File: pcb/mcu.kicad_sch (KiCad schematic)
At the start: 31 parts, among them SW1 SKRKAEE020, U10 W25Q128JVS, U8 RP2040, Y3 ABMM2-12.000MHZ-E2-T

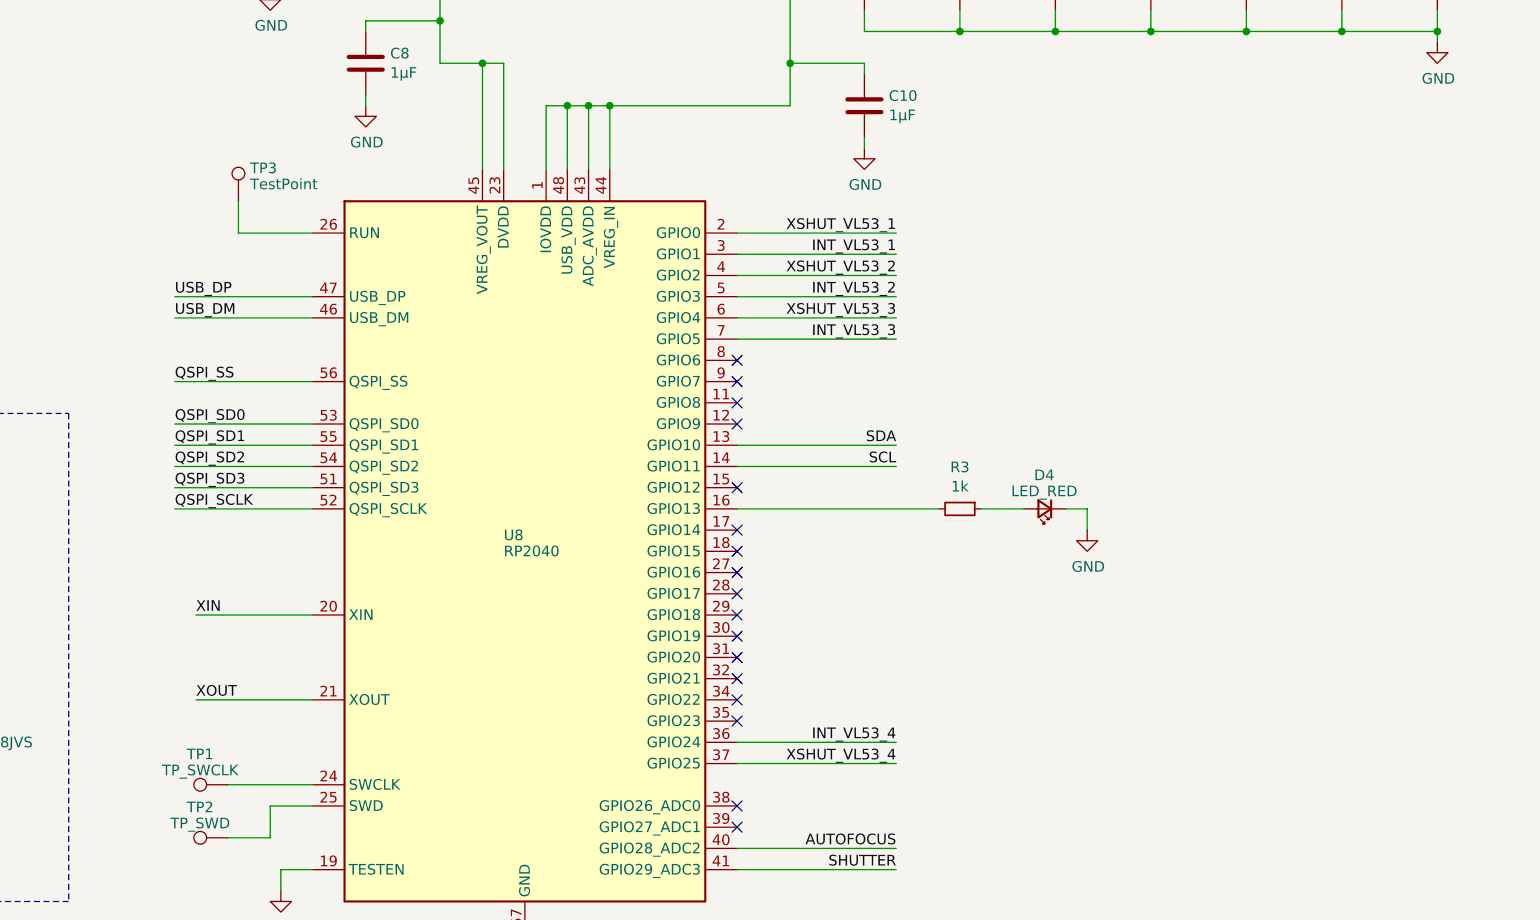
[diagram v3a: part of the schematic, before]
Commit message: refactored components and layout
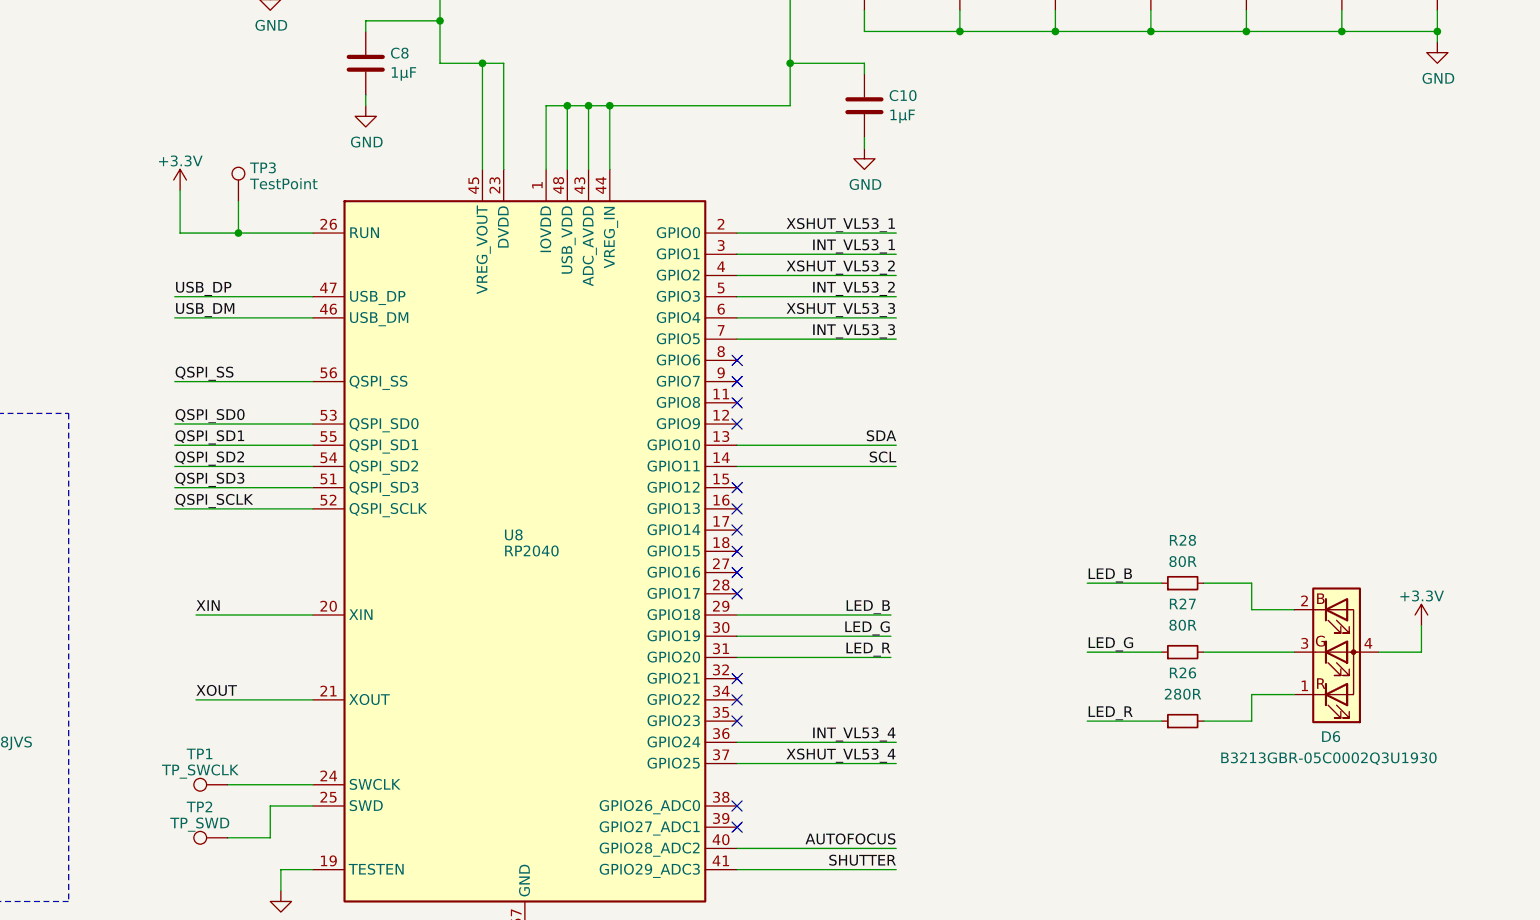
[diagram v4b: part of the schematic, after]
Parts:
- removed D4: LED_RED, LED_SMD:LED_0603_1608Metric, symbol Device:LED_Small
- removed R3: 1k, Resistor_SMD:R_0603_1608Metric, symbol Device:R_Small
- added D6: B3213GBR-05C0002Q3U1930, B3213GBR-05C0002Q3U1930:B3213GBR-05C0002Q3U1930, symbol Device:LED_RBGA
- added R26: 280R, Resistor_SMD:R_0603_1608Metric, symbol Device:R_Small
- added R27, R28: 80R, Resistor_SMD:R_0603_1608Metric, symbol Device:R_Small
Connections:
- net +3.3V: now also TP3.1, U8.26 (RUN), D6.4 (A)
- net LED_B: now reaches U8.29 (GPIO18)
- net LED_B: now also R28.1
- net LED_G: now reaches U8.30 (GPIO19)
- net LED_G: now also R27.1
- net LED_R: now reaches U8.31 (GPIO20)
- net LED_R: now also R26.1
- new net: D6.3 (GK), R27.2
- new net: D6.1 (RK), R26.2
- new net: D6.2 (BK), R28.2
- no-connect marks 17 -> 15

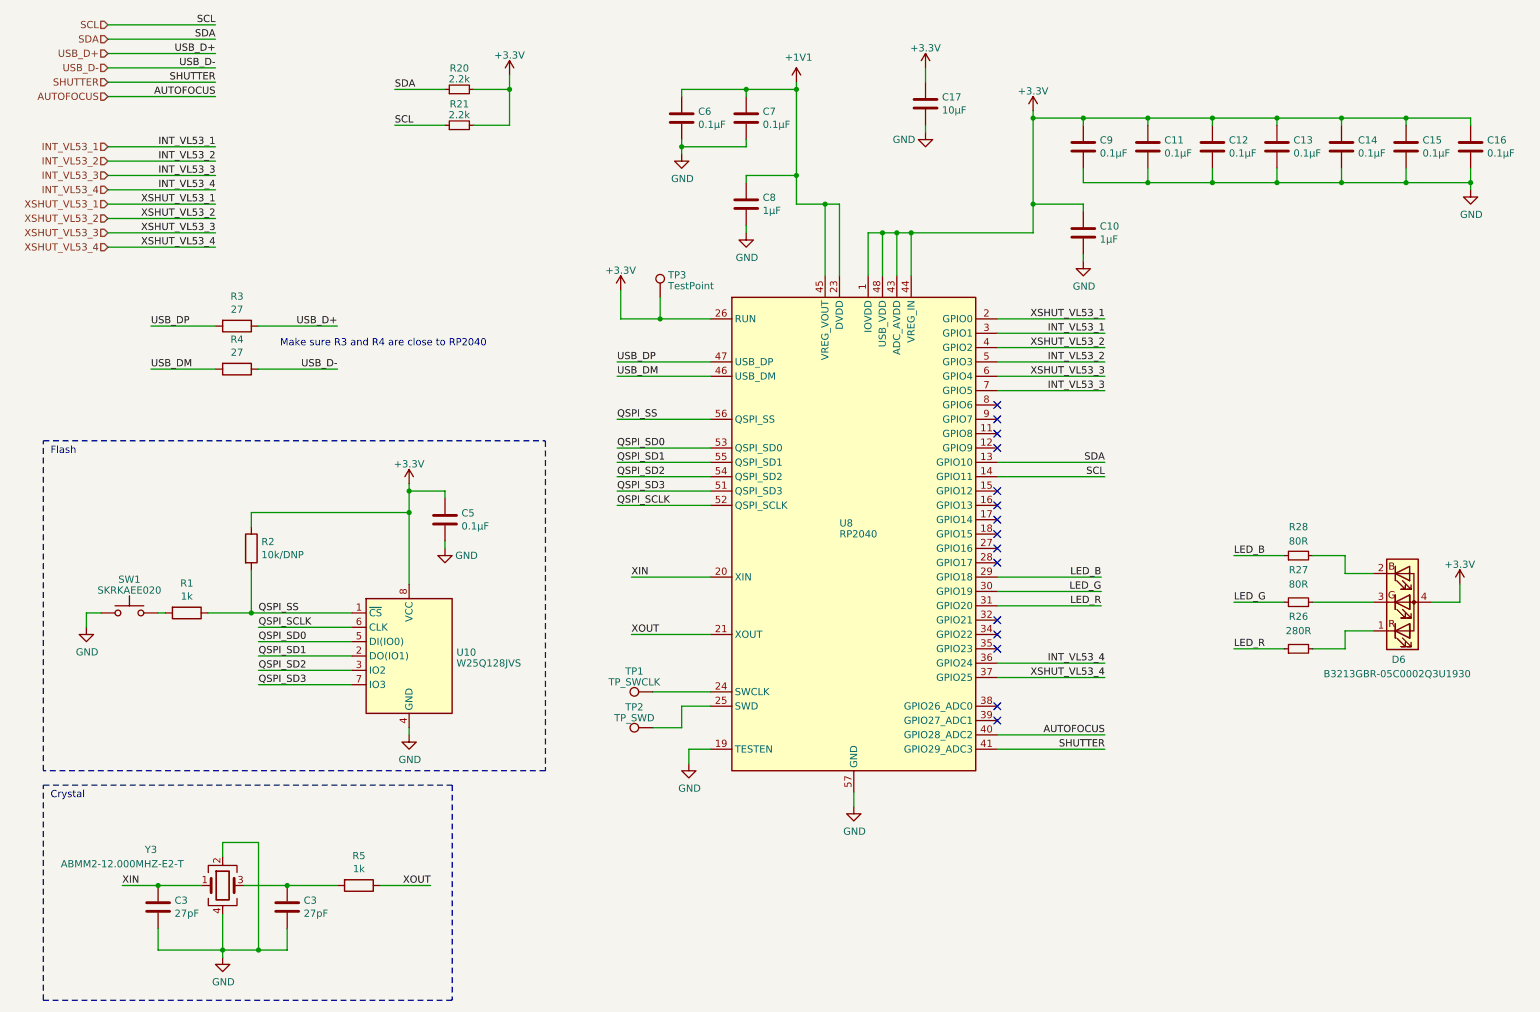
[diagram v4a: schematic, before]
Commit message: re-organise components + added housing data
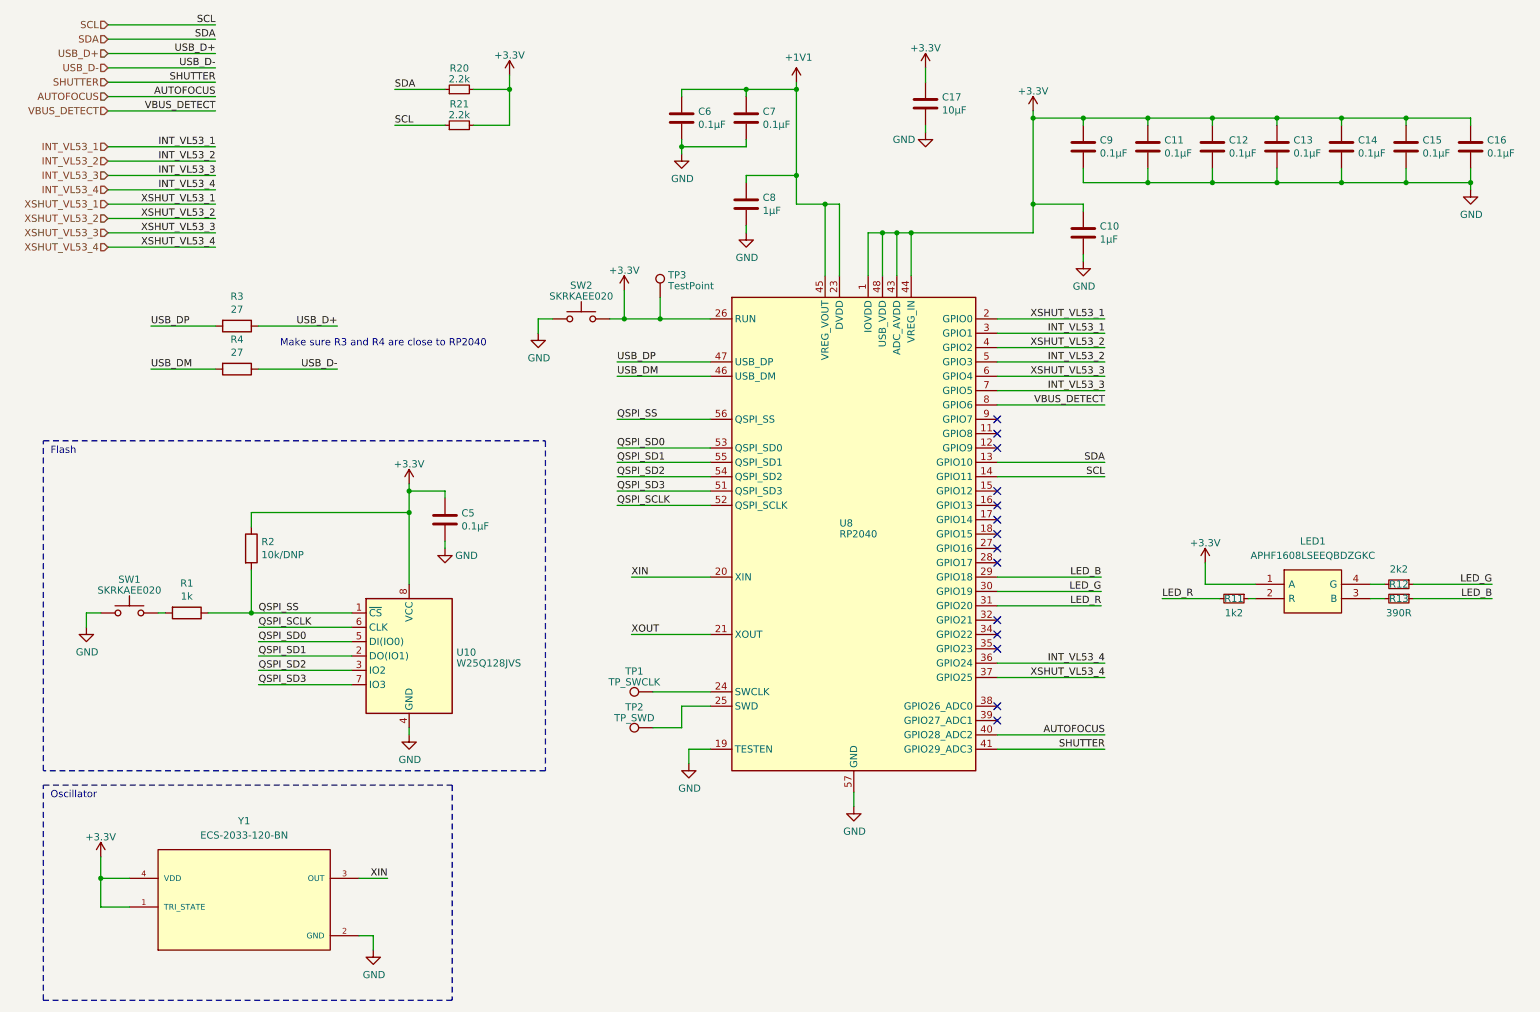
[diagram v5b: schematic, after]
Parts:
- removed C3 (x2): 27pF, Capacitor_SMD:C_0402_1005Metric, symbol Device:C
- removed D6: B3213GBR-05C0002Q3U1930, B3213GBR-05C0002Q3U1930:B3213GBR-05C0002Q3U1930, symbol Device:LED_RBGA
- removed R26: 280R, Resistor_SMD:R_0603_1608Metric, symbol Device:R_Small
- removed R27, R28: 80R, Resistor_SMD:R_0603_1608Metric, symbol Device:R_Small
- removed R5: 1k, Resistor_SMD:R_0603_1608Metric, symbol Device:R
- removed Y3: ABMM2-12.000MHZ-E2-T, ABMM2-12.000MHZ-E2-T:ABMM2, symbol Device:Crystal_GND24
- added LED1: APHF1608LSEEQBDZGKC, APHF1608LSEEQBDZGKC:APHF1608LSEEQBDZGKC, symbol GeniX:APHF1608LSEEQBDZGKC
- added R11: 1k2, Resistor_SMD:R_0603_1608Metric, symbol Device:R_Small
- added R12: 2k2, Resistor_SMD:R_0603_1608Metric, symbol Device:R_Small
- added R13: 390R, Resistor_SMD:R_0603_1608Metric, symbol Device:R_Small
- added SW2: SKRKAEE020, SKRKAEE020:SKRKAEE020, symbol Switch:SW_Push
- added Y1: ECS-2033-120-BN, ECS-2033-120-BN:OSC_ECS-2033-120-BN, symbol GeniX:ECS-2033-120-BN
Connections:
- net +3.3V: now also LED1.1 (A), SW2.2, Y1.1 (TRI_STATE), Y1.4 (VDD)
- net GND: now also SW2.1, Y1.2 (GND)
- net LED_B: now also R13.1
- net LED_G: now also R12.1
- net LED_R: now also R11.2
- net XIN: now also Y1.3 (OUT)
- net VBUS_DETECT: now reaches U8.8 (GPIO6)
- new net: LED1.3 (B), R13.2
- new net: LED1.2 (R), R11.1
- new net: LED1.4 (G), R12.2
- no-connect marks 15 -> 14
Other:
- note added: "Oscillator"
- note removed: "Crystal"

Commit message: Replaced RP2040 with ESP32 + Schematics + Layouting
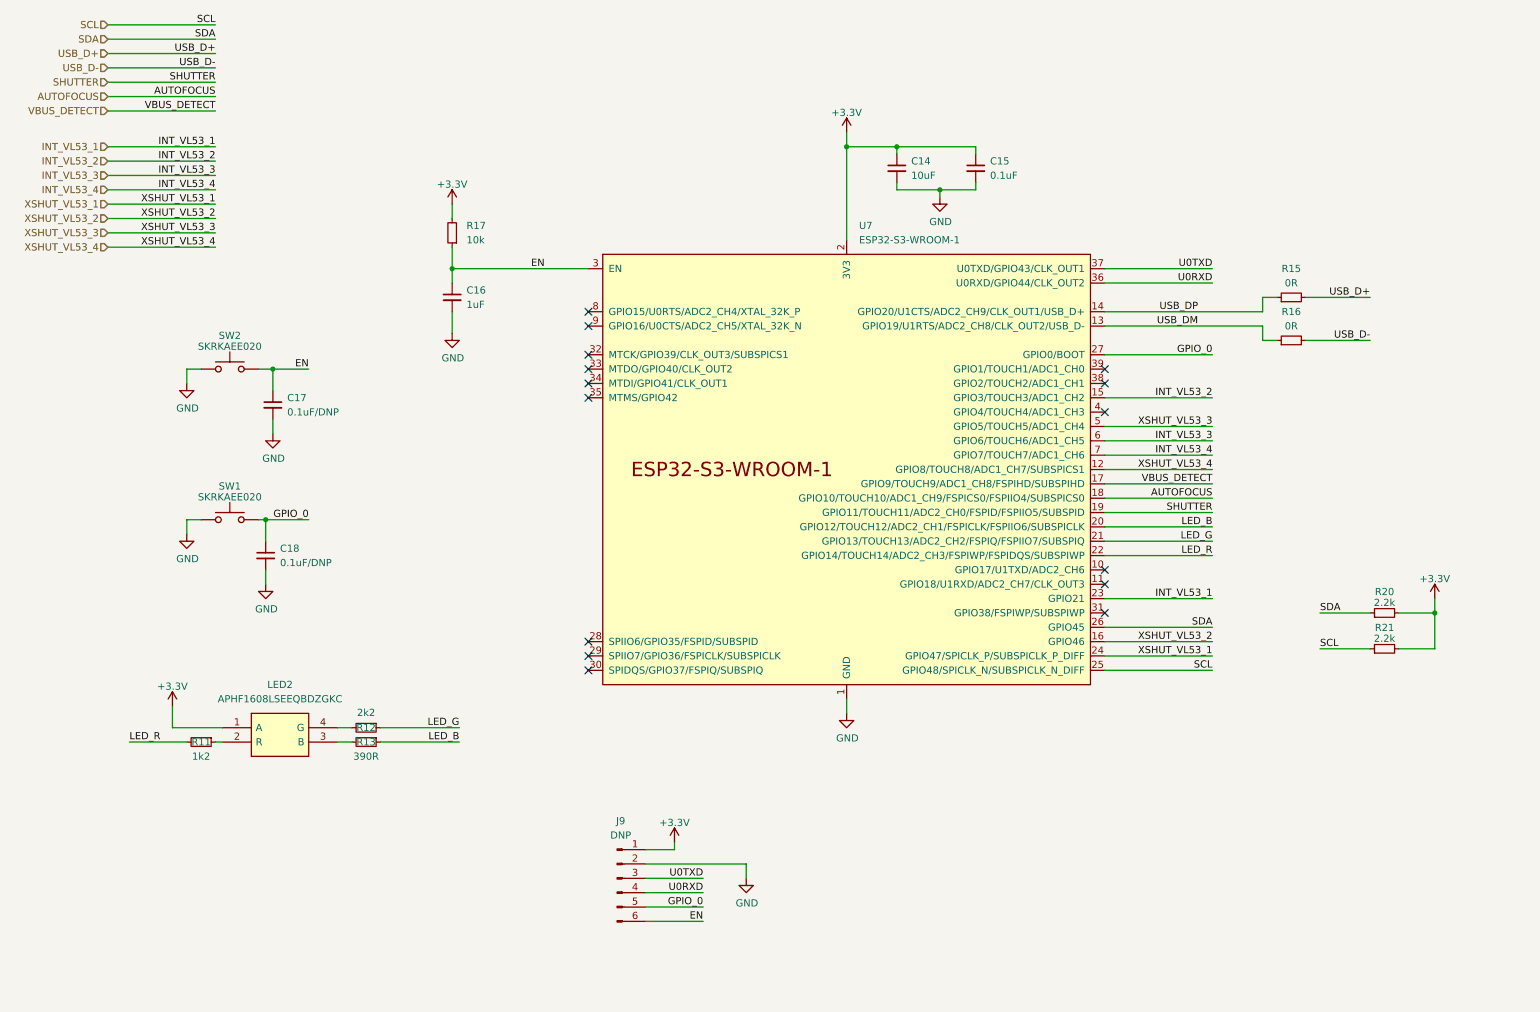
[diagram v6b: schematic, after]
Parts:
- removed C10, C8: 1µF, Capacitor_SMD:C_0402_1005Metric, symbol Device:C
- removed C11, C12, C13, C14, C15, C16, C5, C6, C7, C9: 0.1µF, Capacitor_SMD:C_0402_1005Metric, symbol Device:C
- removed C17: 10µF, Capacitor_SMD:C_0805_2012Metric, symbol Device:C
- removed LED1: APHF1608LSEEQBDZGKC, APHF1608LSEEQBDZGKC:APHF1608LSEEQBDZGKC, symbol GeniX:APHF1608LSEEQBDZGKC
- removed R1: 1k, Resistor_SMD:R_0603_1608Metric, symbol Device:R
- removed R2: 10k/DNP, Resistor_SMD:R_0603_1608Metric, symbol Device:R
- removed R3, R4: 27, Resistor_SMD:R_0402_1005Metric, symbol Device:R
- removed TP1: TP_SWCLK, TestPoint:TestPoint_Pad_D1.5mm, symbol Connector:TestPoint
- removed TP2: TP_SWD, TestPoint:TestPoint_Pad_D1.5mm, symbol Connector:TestPoint
- removed TP3: TestPoint, TestPoint:TestPoint_Pad_D1.5mm, symbol Connector:TestPoint
- removed U10: W25Q128JVS, Package_SO:SOIC-8_5.23x5.23mm_P1.27mm, symbol Memory_Flash:W25Q128JVS
- removed U8: RP2040, Package_DFN_QFN:QFN-56-1EP_7x7mm_P0.4mm_EP3.2x3.2mm, symbol MCU_RaspberryPi:RP2040
- removed Y1: ECS-2033-120-BN, ECS-2033-120-BN:OSC_ECS-2033-120-BN, symbol GeniX:ECS-2033-120-BN
- added C14: 10uF, Capacitor_SMD:C_0603_1608Metric, symbol Device:C_Small
- added C15: 0.1uF, Capacitor_SMD:C_0603_1608Metric, symbol Device:C_Small
- added C16: 1uF, Capacitor_SMD:C_0603_1608Metric, symbol Device:C_Small
- added C17, C18: 0.1uF/DNP, Capacitor_SMD:C_0603_1608Metric, symbol Device:C_Small
- added J9: DNP, Connector_PinSocket_2.54mm:PinSocket_1x06_P2.54mm_Vertical, symbol Connector:Conn_01x06_Pin
- added LED2: APHF1608LSEEQBDZGKC, APHF1608LSEEQBDZGKC:APHF1608LSEEQBDZGKC, symbol APHF1608LSEEQBDZGKC:APHF1608LSEEQBDZGKC
- added R15, R16: 0R, Resistor_SMD:R_0603_1608Metric, symbol Device:R_Small
- added R17: 10k, Resistor_SMD:R_0603_1608Metric, symbol Device:R_Small
- added U7: ESP32-S3-WROOM-1, PCM_Espressif:ESP32-S3-WROOM-1, symbol PCM_Espressif:ESP32-S3-WROOM-1
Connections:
- net +3.3V: now also C14.1, C15.1, J9.1 (Pin_1), LED2.1 (A), R17.2, U7.2 (3V3); no longer SW2.2
- net AUTOFOCUS: now also U7.18 (GPIO10/TOUCH10/ADC1_CH9/FSPICS0/FSPIIO4/SUBSPICS0)
- net GND: now also C14.2, C15.2, C16.2, C17.2, C18.2, J9.2 (Pin_2), U7.1 (GND), U7.40 (GND), U7.41 (GND)
- net INT_VL53_1: now also U7.23 (GPIO21)
- net INT_VL53_2: now also U7.15 (GPIO3/TOUCH3/ADC1_CH2)
- net INT_VL53_3: now also U7.6 (GPIO6/TOUCH6/ADC1_CH5)
- net INT_VL53_4: now also U7.7 (GPIO7/TOUCH7/ADC1_CH6)
- net LED_B: now also U7.20 (GPIO12/TOUCH12/ADC2_CH1/FSPICLK/FSPIIO6/SUBSPICLK)
- net LED_G: now also U7.21 (GPIO13/TOUCH13/ADC2_CH2/FSPIQ/FSPIIO7/SUBSPIQ)
- net LED_R: now also U7.22 (GPIO14/TOUCH14/ADC2_CH3/FSPIWP/FSPIDQS/SUBSPIWP)
- net SCL: now also U7.25 (GPIO48/SPICLK_N/SUBSPICLK_N_DIFF)
- net SDA: now also U7.26 (GPIO45)
- net SHUTTER: now also U7.19 (GPIO11/TOUCH11/ADC2_CH0/FSPID/FSPIIO5/SUBSPID)
- net USB_D+: now also R15.2
- net USB_D-: now also R16.2
- net USB_DM: now also R16.1, U7.13 (GPIO19/U1RTS/ADC2_CH8/CLK_OUT2/USB_D-)
- net USB_DP: now also R15.1, U7.14 (GPIO20/U1CTS/ADC2_CH9/CLK_OUT1/USB_D+)
- net VBUS_DETECT: now also U7.17 (GPIO9/TOUCH9/ADC1_CH8/FSPIHD/SUBSPIHD)
- net XSHUT_VL53_1: now also U7.24 (GPIO47/SPICLK_P/SUBSPICLK_P_DIFF)
- net XSHUT_VL53_2: now also U7.16 (GPIO46)
- net XSHUT_VL53_3: now also U7.5 (GPIO5/TOUCH5/ADC1_CH4)
- net XSHUT_VL53_4: now also U7.12 (GPIO8/TOUCH8/ADC1_CH7/SUBSPICS1)
- net at R13.2: now also LED2.3 (B)
- net at R11.1: now also LED2.2 (R)
- net at R12.2: now also LED2.4 (G)
- net GPIO_0: now reaches SW1.2
- net GPIO_0: now also C18.1, J9.5 (Pin_5), U7.27 (GPIO0/BOOT)
- new net EN: C16.1, C17.1, J9.6 (Pin_6), R17.1, SW2.2, U7.3 (EN)
- new net U0RXD: J9.4 (Pin_4), U7.36 (U0RXD/GPIO44/CLK_OUT2)
- new net U0TXD: J9.3 (Pin_3), U7.37 (U0TXD/GPIO43/CLK_OUT1)
- no-connect marks 14 -> 15
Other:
- note removed: "Flash"
- note removed: "Make sure R3 and R4 are close to RP2040"
- note removed: "Oscillator"
- moved on the sheet: R11, R12, R13, R20, R21, SW2

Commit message: Fixed wrong ESP32-S3 footprint
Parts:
- U7: footprint PCM_Espressif:ESP32-S3-WROOM-1 -> RF_Module:ESP32-S3-WROOM-1
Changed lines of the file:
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@@
       (effects (font (size 1.27 1.27)) (justify left))
     )
-    (property "Footprint" "PCM_Espressif:ESP32-S3-WROOM-1" (at 162.56 143.51 0)
+    (property "Footprint" "RF_Module:ESP32-S3-WROOM-1" (at 162.56 143.51 0)
       (effects (font (size 1.27 1.27)) hide)
     )
